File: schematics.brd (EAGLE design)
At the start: 35.2 x 38.1 mm, 11 parts

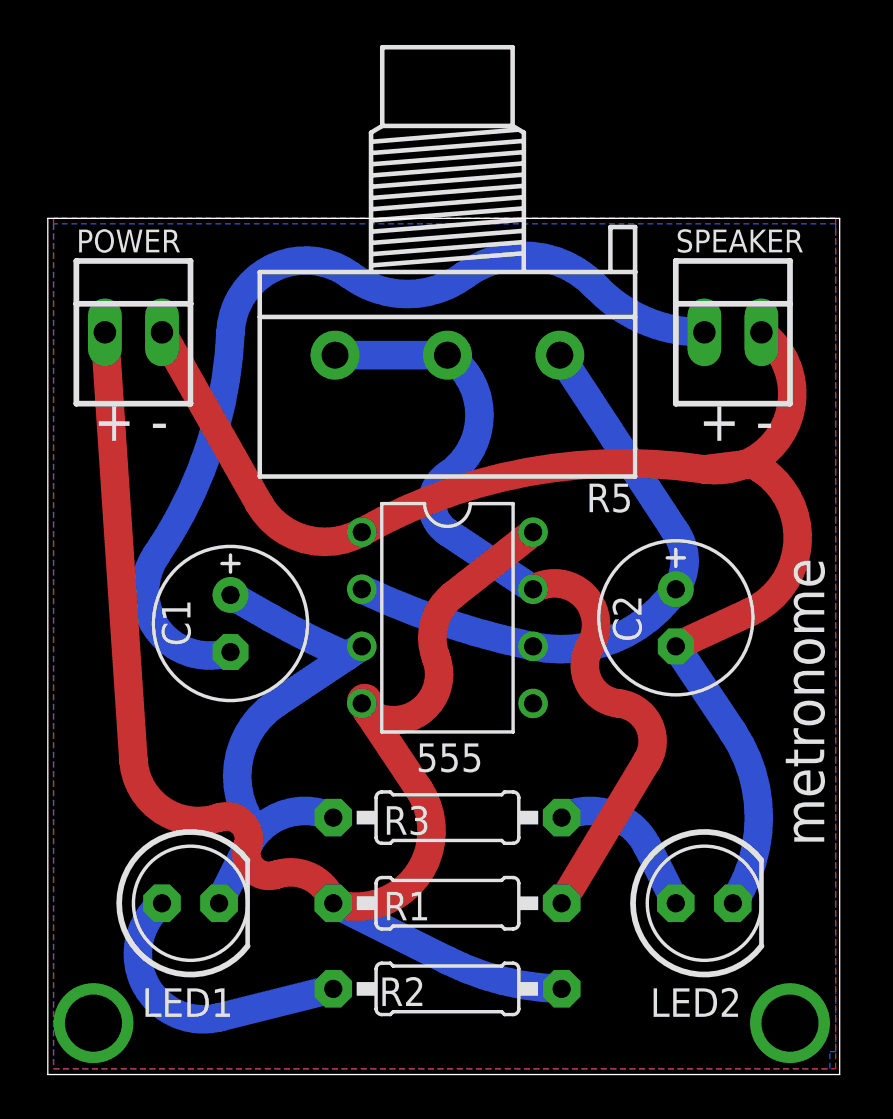
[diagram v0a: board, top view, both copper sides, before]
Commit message: Add round corners.
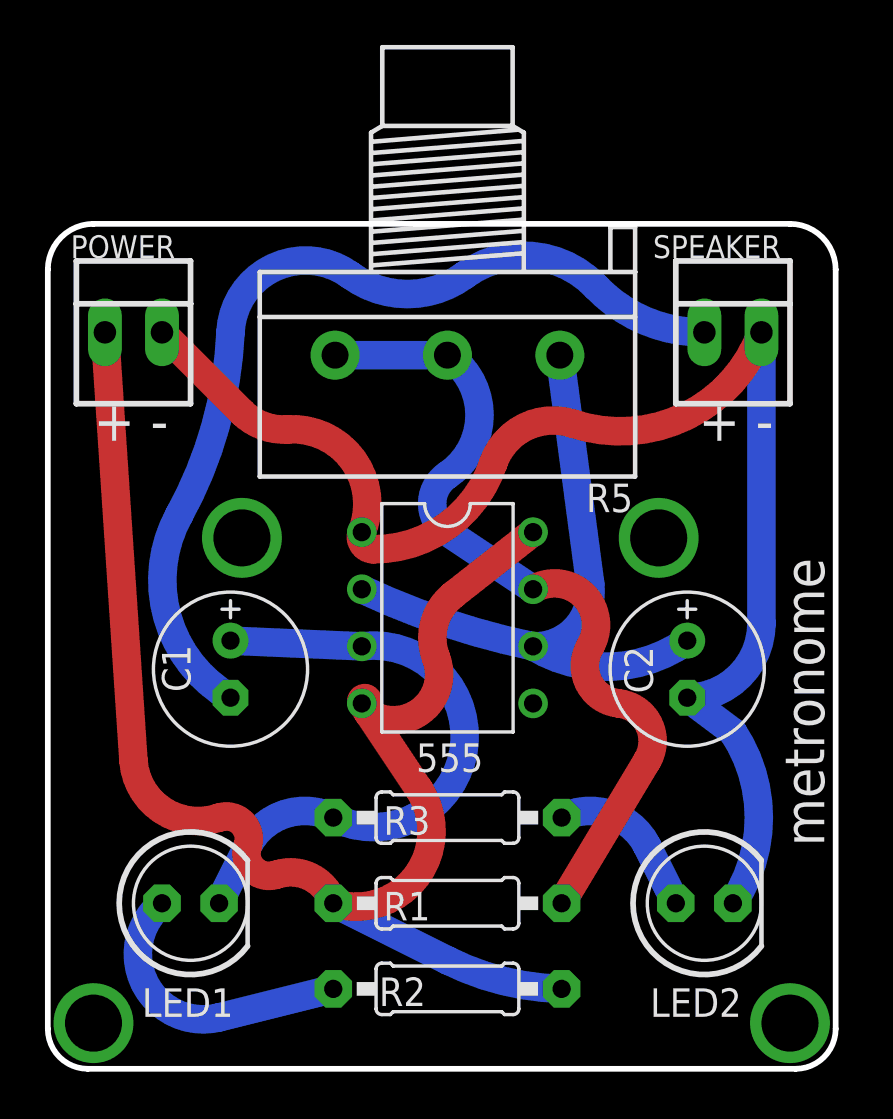
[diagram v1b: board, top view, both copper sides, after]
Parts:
- moved C2 2.34 mm to (55.1, 52.3)
- moved C1 2.03 mm to (34.8, 52.3)
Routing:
- net PIN3: track 22.5 -> 20.4 mm
- net OUTP: track 26.8 -> 28.9 mm
- net N$5: track 38.0 -> 39.0 mm
- net PE: track 60.4 -> 61.4 mm
- removed copper zone on layer 1, net PE
- removed copper zone on layer 16, net PE
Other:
- board size 35.2 x 38.1 mm -> 35.1 x 37.6 mm
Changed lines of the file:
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@@
 <board>
 <plain>
-<wire x1="26.67" y1="34.29" x2="61.9" y2="34.29" width="0" layer="20"/>
-<wire x1="61.9" y1="34.29" x2="61.9" y2="72.38" width="0" layer="20"/>
-<wire x1="61.9" y1="72.38" x2="26.67" y2="72.38" width="0" layer="20"/>
-<wire x1="26.67" y1="72.38" x2="26.67" y2="34.29" width="0" layer="20"/>
 <text x="61.214" y="44.45" size="1.778" layer="21" rot="R90">metronome</text>
 <text x="54.102" y="61.722" size="1.778" layer="22" rot="MR0">danielandrade.net</text>
@@
 <text x="28.702" y="62.484" size="1.778" layer="21">+ -</text>
 <text x="55.626" y="62.484" size="1.778" layer="21">+ -</text>
+<wire x1="26.67" y1="70.104" x2="26.67" y2="36.322" width="0.254" layer="20"/>
+<wire x1="28.448" y1="34.544" x2="59.944" y2="34.544" width="0.254" layer="20"/>
+<wire x1="61.722" y1="36.322" x2="61.722" y2="70.104" width="0.254" layer="20"/>
+<wire x1="59.69" y1="72.136" x2="28.702" y2="72.136" width="0.254" layer="20"/>
+<wire x1="26.67" y1="36.322" x2="28.448" y2="34.544" width="0.254" layer="20" curve="90"/>
+<wire x1="61.722" y1="36.322" x2="59.944" y2="34.544" width="0.254" layer="20" curve="-90"/>
+<wire x1="61.722" y1="70.104" x2="59.69" y2="72.136" width="0.254" layer="20" curve="90"/>
+<wire x1="28.702" y1="72.136" x2="26.67" y2="70.104" width="0.254" layer="20" curve="90"/>
 </plain>
 <attributes>
@@
 </autorouter>
 <elements>
-<element name="C1" library="resistor" package="E2,5-7" value="22uF" x="34.798" y="54.356" smashed="yes" rot="R270">
-<attribute name="NAME" x="33.02" y="53.34" size="1.27" layer="25" ratio="10" rot="R90"/>
-<attribute name="VALUE" x="33.274" y="49.403" size="1.27" layer="27" ratio="10"/>
-</element>
-<element name="C2" library="resistor" package="E2,5-7" value="22uF" x="54.61" y="54.61" smashed="yes" rot="R270">
-<attribute name="NAME" x="51.816" y="55.626" size="1.27" layer="25" ratio="10" rot="R270"/>
-<attribute name="VALUE" x="52.578" y="49.657" size="1.27" layer="27" ratio="10"/>
+<element name="C1" library="resistor" package="E2,5-7" value="22uF" x="34.798" y="52.324" smashed="yes" rot="R270">
+<attribute name="NAME" x="33.02" y="51.308" size="1.27" layer="25" ratio="10" rot="R90"/>
+<attribute name="VALUE" x="33.274" y="47.371" size="1.27" layer="27" ratio="10"/>
+</element>
+<element name="C2" library="resistor" package="E2,5-7" value="22uF" x="55.118" y="52.324" smashed="yes" rot="R270">
+<attribute name="NAME" x="52.324" y="53.34" size="1.27" layer="25" ratio="10" rot="R270"/>
+<attribute name="VALUE" x="53.086" y="47.371" size="1.27" layer="27" ratio="10"/>
 </element>
 <element name="555" library="linear" package="DIL08" value="LM555N" x="44.45" y="54.61" smashed="yes" rot="R270">
@@
 <attribute name="MF" value="MOLEX" x="30.48" y="67.31" size="1.778" layer="27" display="off"/>
 <attribute name="MPN" value="22-23-2021" x="30.48" y="67.31" size="1.778" layer="27" display="off"/>
-<attribute name="NAME" x="27.94" y="70.866" size="1.016" layer="25" ratio="10"/>
+<attribute name="NAME" x="27.686" y="70.612" size="1.016" layer="25" ratio="10"/>
 <attribute name="VALUE" x="26.162" y="64.77" size="1.016" layer="27" ratio="10" rot="R90"/>
 </element>
@@
 <attribute name="MF" value="MOLEX" x="57.15" y="67.31" size="1.778" layer="27" display="off"/>
 <attribute name="MPN" value="22-23-2021" x="57.15" y="67.31" size="1.778" layer="27" display="off"/>
-<attribute name="NAME" x="54.61" y="70.866" size="1.016" layer="25" ratio="10"/>
+<attribute name="NAME" x="53.594" y="70.612" size="1.016" layer="25" ratio="10"/>
 <attribute name="VALUE" x="63.246" y="65.024" size="1.016" layer="27" ratio="10" rot="R90"/>
 </element>
@@
 <contactref element="555" pad="2"/>
 <contactref element="555" pad="6"/>
-<wire x1="54.61" y1="58.42" x2="54.61" y2="55.88" width="1.27" layer="16" curve="-69.270556"/>
-<wire x1="54.61" y1="55.88" x2="48.26" y2="53.34" width="1.27" layer="16" curve="-67.126602"/>
+<wire x1="55.118" y1="53.594" x2="48.26" y2="53.34" width="1.27" layer="16" curve="-67.126602"/>
 <wire x1="48.26" y1="53.34" x2="40.64" y2="55.88" width="1.27" layer="16" curve="-13.346104"/>
 <contactref element="R5" pad="1"/>
-<wire x1="49.45" y1="66.294" x2="54.61" y2="58.42" width="1.27" layer="16"/>
+<wire x1="49.45" y1="66.294" x2="50.8" y2="56.134" width="1.27" layer="16"/>
+<wire x1="50.8" y1="56.134" x2="48.26" y2="53.34" width="1.27" layer="16" curve="-99.684945"/>
 </signal>
 <signal name="PE">
@@
 <contactref element="555" pad="1"/>
 <contactref element="POWER" pad="2"/>
-<wire x1="31.75" y1="67.31" x2="36.068" y2="59.69" width="1.27" layer="1"/>
-<wire x1="36.068" y1="59.69" x2="40.64" y2="58.42" width="1.27" layer="1" curve="89.874186"/>
-<wire x1="40.64" y1="58.42" x2="55.88" y2="61.214" width="1.27" layer="1" curve="-38.048221"/>
-<wire x1="55.88" y1="61.214" x2="58.42" y2="67.31" width="1.27" layer="1" curve="152.030729"/>
-<wire x1="54.61" y1="53.34" x2="57.912" y2="54.864" width="1.27" layer="1"/>
-<wire x1="57.912" y1="54.864" x2="58.42" y2="61.214" width="1.27" layer="1" curve="121.301885"/>
-<wire x1="58.42" y1="61.214" x2="57.912" y2="61.468" width="1.27" layer="1" curve="14.715849"/>
-<wire x1="54.61" y1="53.34" x2="57.15" y2="49.53" width="1.27" layer="16"/>
-<wire x1="55.88" y1="61.214" x2="57.912" y2="61.468" width="1.27" layer="1"/>
-<polygon width="0.254" layer="1">
-<vertex x="26.924" y="72.136"/>
-<vertex x="26.924" y="34.544"/>
-<vertex x="61.722" y="34.544"/>
-<vertex x="61.722" y="38.354"/>
-<vertex x="61.722" y="72.39"/>
-<vertex x="26.924" y="72.39"/>
-</polygon>
-<polygon width="0.254" layer="16">
-<vertex x="26.924" y="72.136"/>
-<vertex x="26.924" y="34.544"/>
-<vertex x="61.468" y="34.544"/>
-<vertex x="61.468" y="35.306"/>
-<vertex x="61.722" y="35.306"/>
-<vertex x="61.722" y="71.882"/>
-<vertex x="61.722" y="72.136"/>
-</polygon>
+<wire x1="55.118" y1="51.054" x2="57.15" y2="49.53" width="1.27" layer="16"/>
+<wire x1="58.42" y1="67.31" x2="58.42" y2="54.356" width="1.27" layer="16"/>
+<wire x1="58.42" y1="54.356" x2="55.118" y2="51.054" width="1.27" layer="16" curve="-90"/>
+<wire x1="31.75" y1="67.31" x2="35.306" y2="63.754" width="1.27" layer="1"/>
+<wire x1="35.306" y1="63.754" x2="37.338" y2="62.992" width="1.27" layer="1" curve="48.88791"/>
+<wire x1="37.338" y1="62.992" x2="40.64" y2="58.42" width="1.27" layer="1" curve="-116.100759"/>
+<wire x1="40.64" y1="58.42" x2="41.148" y2="57.658" width="1.27" layer="1" curve="111.805731"/>
+<wire x1="41.148" y1="57.658" x2="46.482" y2="61.468" width="1.27" layer="1" curve="71.890396"/>
+<wire x1="46.482" y1="61.468" x2="50.038" y2="63.246" width="1.27" layer="1" curve="-89.835688"/>
+<wire x1="50.038" y1="63.246" x2="58.42" y2="67.31" width="1.27" layer="1" curve="88.438343"/>
 </signal>
 <signal name="N$1">
@@
 <wire x1="34.29" y1="41.91" x2="35.56" y2="44.45" width="1.27" layer="16"/>
 <wire x1="35.56" y1="44.45" x2="39.37" y2="45.72" width="1.27" layer="16" curve="-90"/>
-<wire x1="40.64" y1="53.34" x2="39.99523125" y2="52.910153125" width="1.27" layer="16"/>
-<wire x1="39.99523125" y1="52.910153125" x2="36.83" y2="50.8" width="1.27" layer="16"/>
-<wire x1="36.83" y1="50.8" x2="35.56" y2="45.72" width="1.27" layer="16" curve="84.547378"/>
-<wire x1="34.798" y1="55.626" x2="36.576" y2="54.61" width="1.27" layer="16"/>
-<wire x1="36.576" y1="54.61" x2="39.99523125" y2="52.910153125" width="1.27" layer="16" curve="6.621868"/>
-<wire x1="35.56" y1="44.45" x2="35.56" y2="45.72" width="0" layer="19" extent="16-16"/>
+<wire x1="34.798" y1="53.594" x2="40.64" y2="53.34" width="1.27" layer="16"/>
+<wire x1="39.37" y1="45.72" x2="40.64" y2="53.34" width="1.27" layer="16" curve="214.205432"/>
 </signal>
 <signal name="N$4">
@@
 <wire x1="45.212" y1="69.85" x2="51.054" y2="69.342" width="1.27" layer="16" curve="-82.996489"/>
 <wire x1="51.054" y1="69.342" x2="55.88" y2="67.31" width="1.27" layer="16" curve="47.268681"/>
-<wire x1="34.798" y1="67.31" x2="31.496" y2="57.404" width="1.27" layer="16" curve="-31.780267"/>
-<wire x1="31.496" y1="57.404" x2="34.798" y2="53.086" width="1.27" layer="16" curve="143.460827"/>
-</signal>
-<signal name="N$2">
+<wire x1="34.798" y1="67.31" x2="32.512" y2="59.182" width="1.27" layer="16" curve="-26.327644"/>
+<wire x1="32.512" y1="59.182" x2="34.798" y2="51.054" width="1.27" layer="16" curve="89.162177"/>
+</signal>
+<signal name="GND">
 <via x="28.702" y="36.576" extent="1-16" drill="2.54"/>
-</signal>
-<signal name="N$6">
+<via x="35.306" y="58.166" extent="1-16" drill="2.54"/>
+<via x="53.848" y="58.166" extent="1-16" drill="2.54"/>
 <via x="59.69" y="36.576" extent="1-16" drill="2.54"/>
+<wire x1="35.306" y1="58.166" x2="53.848" y2="58.166" width="0" layer="19" extent="1-1"/>
+<wire x1="59.69" y1="36.576" x2="53.848" y2="58.166" width="0" layer="19" extent="1-1"/>
+<wire x1="28.702" y1="36.576" x2="35.306" y2="58.166" width="0" layer="19" extent="1-1"/>
 </signal>
 </signals>

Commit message: Ground place.
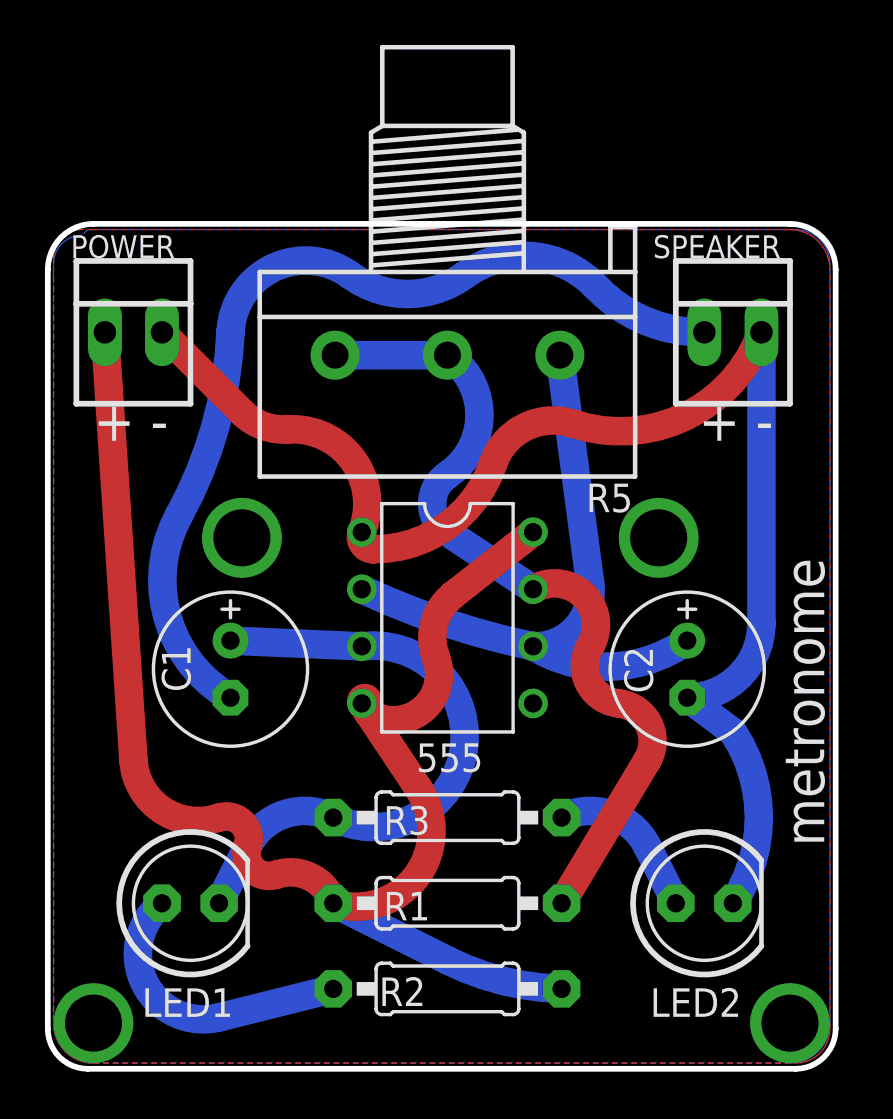
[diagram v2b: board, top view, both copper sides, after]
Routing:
- added copper zone on layer 1, net GND
- added copper zone on layer 16, net N$2
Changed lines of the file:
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@@
 <via x="53.848" y="58.166" extent="1-16" drill="2.54"/>
 <via x="59.69" y="36.576" extent="1-16" drill="2.54"/>
-<wire x1="35.306" y1="58.166" x2="53.848" y2="58.166" width="0" layer="19" extent="1-1"/>
-<wire x1="59.69" y1="36.576" x2="53.848" y2="58.166" width="0" layer="19" extent="1-1"/>
-<wire x1="28.702" y1="36.576" x2="35.306" y2="58.166" width="0" layer="19" extent="1-1"/>
+<polygon width="0.254" layer="1">
+<vertex x="26.924" y="70.612"/>
+<vertex x="26.924" y="36.576" curve="90"/>
+<vertex x="28.702" y="34.798"/>
+<vertex x="59.944" y="34.798" curve="90"/>
+<vertex x="61.468" y="36.322"/>
+<vertex x="61.468" y="70.104" curve="90"/>
+<vertex x="59.69" y="71.882"/>
+<vertex x="28.702" y="71.882"/>
+<vertex x="28.194" y="71.882" curve="90"/>
+</polygon>
+</signal>
+<signal name="N$2">
+<polygon width="0.254" layer="16">
+<vertex x="26.924" y="69.85"/>
+<vertex x="26.924" y="36.576" curve="90"/>
+<vertex x="28.702" y="34.798"/>
+<vertex x="59.69" y="34.798" curve="90"/>
+<vertex x="61.468" y="36.576"/>
+<vertex x="61.468" y="70.358" curve="90"/>
+<vertex x="59.944" y="71.882"/>
+<vertex x="28.448" y="71.882"/>
+<vertex x="28.194" y="71.628" curve="90"/>
+<vertex x="26.924" y="70.358"/>
+</polygon>
 </signal>
 </signals>
